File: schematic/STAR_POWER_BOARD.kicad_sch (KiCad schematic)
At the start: 62 parts, among them J1 1017491, J14 1017491, J19 6120XX21621_61200821621, J2 6120XX21621_61200621621, J21 6120XX21621_61200621621, Q1 CSD18540Q5B, Q2 CSD17577Q3A, Q3 CSD17577Q3A, Q4 CSD18540Q5B, U1 TPS566238PRQFR, U2 TPS566238PRQFR, U3 TPS40305DRCT

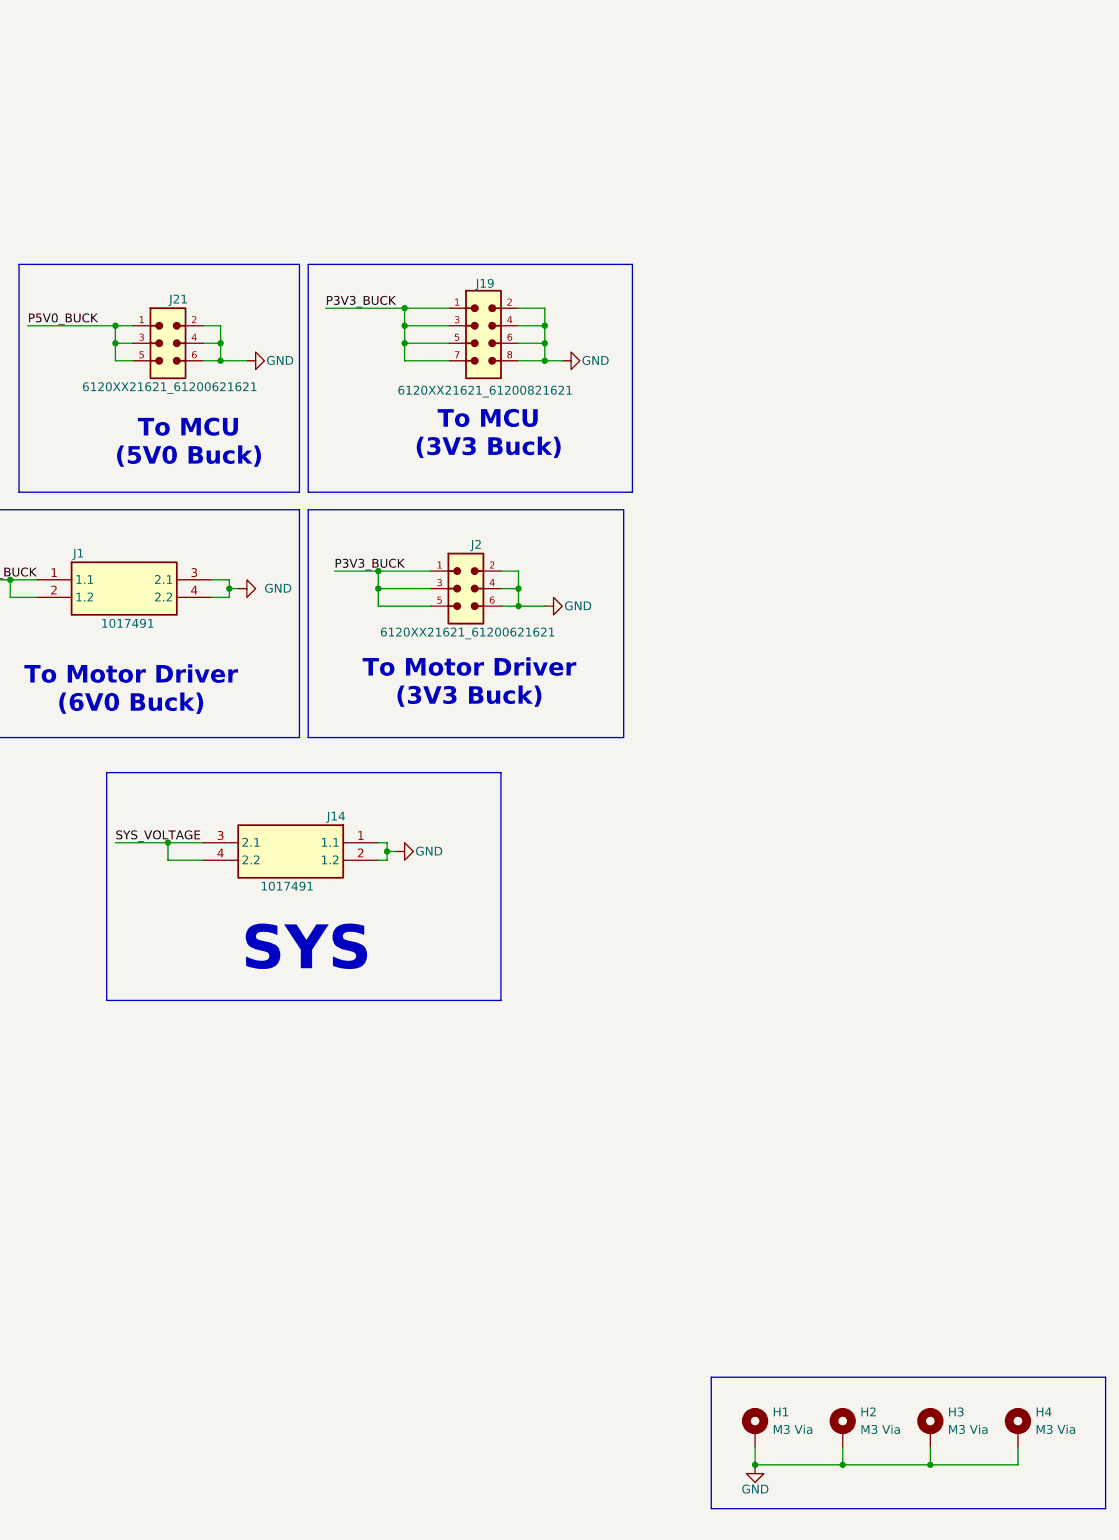
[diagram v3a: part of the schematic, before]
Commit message: Add missing footprint libraries and fix schematic references
Register three missing footprint libraries in fp-lib-table:
- DNK0008A (transistor package)
- INDPM110100X400N (inductor package)
- Q3A (transistor package)

Update STAR_POWER_BOARD schematic to use library-prefixed footprint references:
- L3: INDPM110100X400N:INDPM110100X400N
- Q1, Q4: DNK0008A:DNK0008A
- Q2, Q3: Q3A:Q3A

Fixes "footprint not found" errors during PCB update.
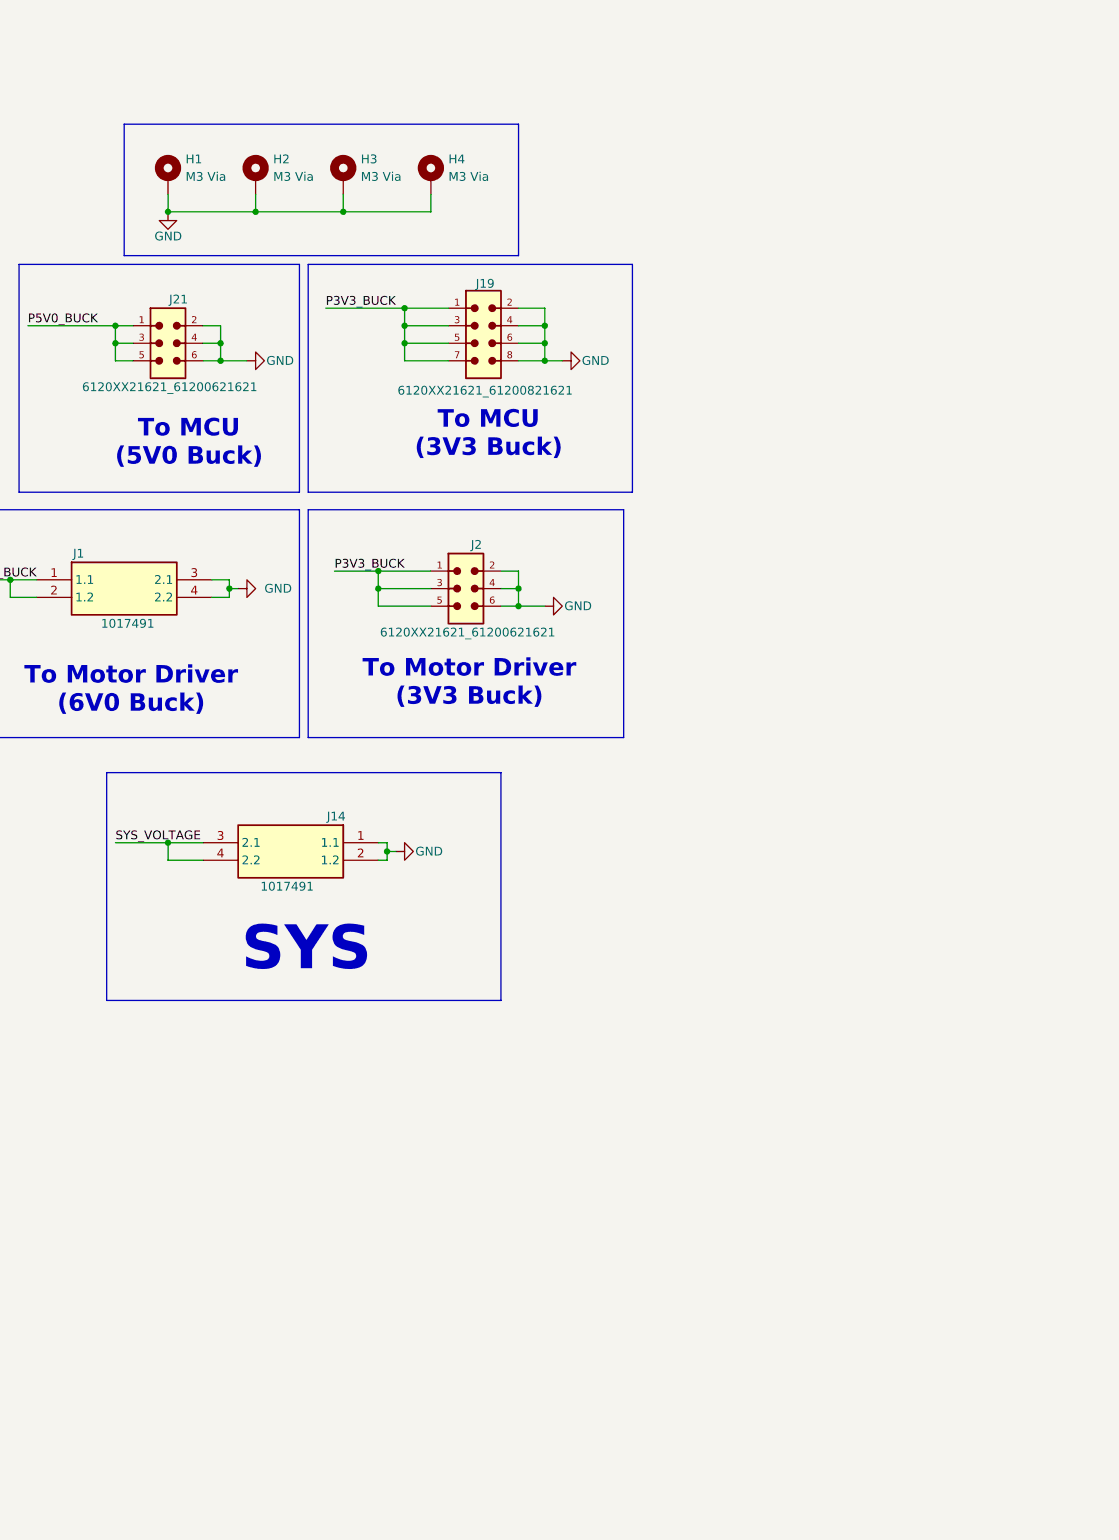
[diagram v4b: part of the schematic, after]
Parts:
- C33: footprint CAPC7866X950N:CAPC7866X950N -> CAPC7866X950N
- L3: footprint INDPM110100X400N -> INDPM110100X400N:INDPM110100X400N
- Q1, Q4: footprint DNK0008A -> DNK0008A:DNK0008A
- Q2, Q3: footprint Q3A -> Q3A:Q3A
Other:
- moved on the sheet: H1, H2, H3, H4
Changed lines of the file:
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@@
 	)
 	(rectangle
-		(start 347.98 229.87)
-		(end 405.13 248.92)
+		(start 262.89 48.26)
+		(end 320.04 67.31)
 		(stroke
 			(width 0)
@@
 	)
 	(junction
-		(at 354.33 242.57)
+		(at 269.24 60.96)
 		(diameter 0)
 		(color 0 0 0 0)
@@
 	)
 	(junction
-		(at 379.73 242.57)
+		(at 294.64 60.96)
 		(diameter 0)
 		(color 0 0 0 0)
@@
 	)
 	(junction
-		(at 367.03 242.57)
+		(at 281.94 60.96)
 		(diameter 0)
 		(color 0 0 0 0)
@@
 	(wire
 		(pts
-			(xy 392.43 240.03) (xy 392.43 242.57)
+			(xy 307.34 58.42) (xy 307.34 60.96)
 		)
 		(stroke
@@
 	(wire
 		(pts
-			(xy 354.33 240.03) (xy 354.33 242.57)
+			(xy 269.24 58.42) (xy 269.24 60.96)
 		)
 		(stroke
@@
 	(wire
 		(pts
-			(xy 367.03 242.57) (xy 354.33 242.57)
+			(xy 281.94 60.96) (xy 269.24 60.96)
 		)
 		(stroke
@@
 	(wire
 		(pts
-			(xy 392.43 242.57) (xy 379.73 242.57)
+			(xy 307.34 60.96) (xy 294.64 60.96)
 		)
 		(stroke
@@
 	(wire
 		(pts
-			(xy 367.03 242.57) (xy 379.73 242.57)
+			(xy 281.94 60.96) (xy 294.64 60.96)
 		)
 		(stroke
@@
 	(wire
 		(pts
-			(xy 379.73 240.03) (xy 379.73 242.57)
+			(xy 294.64 58.42) (xy 294.64 60.96)
 		)
 		(stroke
@@
 	(wire
 		(pts
-			(xy 367.03 240.03) (xy 367.03 242.57)
+			(xy 281.94 58.42) (xy 281.94 60.96)
 		)
 		(stroke
@@
 	(symbol
 		(lib_id "power:GND")
-		(at 354.33 242.57 0)
+		(at 269.24 60.96 0)
 		(unit 1)
 		(exclude_from_sim no)
@@
 		(dnp no)
 		(property "Reference" "#PWR01"
-			(at 354.33 248.92 0)
+			(at 269.24 67.31 0)
 			(effects
 				(font
@@
 		)
 		(property "Value" "GND"
-			(at 356.362 246.126 0)
+			(at 271.272 64.516 0)
 			(effects
 				(font
@@
 		)
 		(property "Footprint" ""
-			(at 354.33 242.57 0)
+			(at 269.24 60.96 0)
 			(effects
 				(font
@@
 		)
 		(property "Datasheet" ""
-			(at 354.33 242.57 0)
+			(at 269.24 60.96 0)
 			(effects
 				(font
@@
 		)
 		(property "Description" "Power symbol creates a global label with name \"GND\" , ground"
-			(at 354.33 242.57 0)
+			(at 269.24 60.96 0)
 			(effects
 				(font
@@
 			)
 		)
-		(property "Footprint" "Q3A"
+		(property "Footprint" "Q3A:Q3A"
 			(at 154.94 317.17 0)
 			(effects
@@
 	(symbol
 		(lib_id "Mechanical:MountingHole_Pad")
-		(at 367.03 237.49 0)
+		(at 281.94 55.88 0)
 		(unit 1)
 		(exclude_from_sim no)
@@
 		(fields_autoplaced yes)
 		(property "Reference" "H2"
-			(at 369.57 234.9499 0)
+			(at 284.48 53.3399 0)
 			(effects
 				(font
@@
 		)
 		(property "Value" "M3 Via"
-			(at 369.57 237.4899 0)
+			(at 284.48 55.8799 0)
 			(effects
 				(font
@@
 		)
 		(property "Footprint" "MountingHole:MountingHole_3.2mm_M3_Pad_Via"
-			(at 367.03 237.49 0)
+			(at 281.94 55.88 0)
 			(effects
 				(font
@@
 		)
 		(property "Datasheet" "~"
-			(at 367.03 237.49 0)
+			(at 281.94 55.88 0)
 			(effects
 				(font
@@
 		)
 		(property "Description" "Mounting Hole with connection"
-			(at 367.03 237.49 0)
+			(at 281.94 55.88 0)
 			(effects
 				(font
@@
 		)
 		(property "SNAPEDA_PN" ""
-			(at 367.03 237.49 0)
+			(at 281.94 55.88 0)
 			(effects
 				(font
@@
 		)
 		(property "Sim.Type" ""
-			(at 367.03 237.49 0)
+			(at 281.94 55.88 0)
 			(effects
 				(font
@@
 	(symbol
 		(lib_id "Mechanical:MountingHole_Pad")
-		(at 392.43 237.49 0)
+		(at 307.34 55.88 0)
 		(unit 1)
 		(exclude_from_sim no)
@@
 		(fields_autoplaced yes)
 		(property "Reference" "H4"
-			(at 394.97 234.9499 0)
+			(at 309.88 53.3399 0)
 			(effects
 				(font
@@
 		)
 		(property "Value" "M3 Via"
-			(at 394.97 237.4899 0)
+			(at 309.88 55.8799 0)
 			(effects
 				(font
@@
 		)
 		(property "Footprint" "MountingHole:MountingHole_3.2mm_M3_Pad_Via"
-			(at 392.43 237.49 0)
+			(at 307.34 55.88 0)
 			(effects
 				(font
@@
 		)
 		(property "Datasheet" "~"
-			(at 392.43 237.49 0)
+			(at 307.34 55.88 0)
 			(effects
 				(font
@@
 		)
 		(property "Description" "Mounting Hole with connection"
-			(at 392.43 237.49 0)
+			(at 307.34 55.88 0)
 			(effects
 				(font
@@
 		)
 		(property "SNAPEDA_PN" ""
-			(at 392.43 237.49 0)
+			(at 307.34 55.88 0)
 			(effects
 				(font
@@
 		)
 		(property "Sim.Type" ""
-			(at 392.43 237.49 0)
+			(at 307.34 55.88 0)
 			(effects
 				(font
@@
 	(symbol
 		(lib_id "Mechanical:MountingHole_Pad")
-		(at 379.73 237.49 0)
+		(at 294.64 55.88 0)
 		(unit 1)
 		(exclude_from_sim no)
@@
 		(fields_autoplaced yes)
 		(property "Reference" "H3"
-			(at 382.27 234.9499 0)
+			(at 297.18 53.3399 0)
 			(effects
 				(font
@@
 		)
 		(property "Value" "M3 Via"
-			(at 382.27 237.4899 0)
+			(at 297.18 55.8799 0)
 			(effects
 				(font
@@
 		)
 		(property "Footprint" "MountingHole:MountingHole_3.2mm_M3_Pad_Via"
-			(at 379.73 237.49 0)
+			(at 294.64 55.88 0)
 			(effects
 				(font
@@
 		)
 		(property "Datasheet" "~"
-			(at 379.73 237.49 0)
+			(at 294.64 55.88 0)
 			(effects
 				(font
@@
 		)
 		(property "Description" "Mounting Hole with connection"
-			(at 379.73 237.49 0)
+			(at 294.64 55.88 0)
 			(effects
 				(font
@@
 		)
 		(property "SNAPEDA_PN" ""
-			(at 379.73 237.49 0)
+			(at 294.64 55.88 0)
 			(effects
 				(font
@@
 		)
 		(property "Sim.Type" ""
-			(at 379.73 237.49 0)
+			(at 294.64 55.88 0)
 			(effects
 				(font
@@
 			)
 		)
-		(property "Footprint" "INDPM110100X400N"
+		(property "Footprint" "INDPM110100X400N:INDPM110100X400N"
 			(at 166.37 201.93 0)
 			(effects
@@
 			)
 		)
-		(property "Footprint" "CAPC7866X950N:CAPC7866X950N"
+		(property "Footprint" "CAPC7866X950N"
 			(at 199.0852 229.87 0)
 			(effects
@@
 			)
 		)
-		(property "Footprint" "DNK0008A"
+		(property "Footprint" "DNK0008A:DNK0008A"
 			(at 175.26 286.69 0)
 			(effects
@@
 			)
 		)
-		(property "Footprint" "DNK0008A"
+		(property "Footprint" "DNK0008A:DNK0008A"
 			(at 154.94 286.69 0)
 			(effects
@@
 			)
 		)
-		(property "Footprint" "Q3A"
+		(property "Footprint" "Q3A:Q3A"
 			(at 170.18 308.28 0)
 			(effects
@@
 	(symbol
 		(lib_id "Mechanical:MountingHole_Pad")
-		(at 354.33 237.49 0)
+		(at 269.24 55.88 0)
 		(unit 1)
 		(exclude_from_sim no)
@@
 		(fields_autoplaced yes)
 		(property "Reference" "H1"
-			(at 356.87 234.9499 0)
+			(at 271.78 53.3399 0)
 			(effects
 				(font
@@
 		)
 		(property "Value" "M3 Via"
-			(at 356.87 237.4899 0)
+			(at 271.78 55.8799 0)
 			(effects
 				(font
@@
 		)
 		(property "Footprint" "MountingHole:MountingHole_3.2mm_M3_Pad_Via"
-			(at 354.33 237.49 0)
+			(at 269.24 55.88 0)
 			(effects
 				(font
@@
 		)
 		(property "Datasheet" "~"
-			(at 354.33 237.49 0)
+			(at 269.24 55.88 0)
 			(effects
 				(font
@@
 		)
 		(property "Description" "Mounting Hole with connection"
-			(at 354.33 237.49 0)
+			(at 269.24 55.88 0)
 			(effects
 				(font
@@
 		)
 		(property "SNAPEDA_PN" ""
-			(at 354.33 237.49 0)
+			(at 269.24 55.88 0)
 			(effects
 				(font
@@
 		)
 		(property "Sim.Type" ""
-			(at 354.33 237.49 0)
+			(at 269.24 55.88 0)
 			(effects
 				(font

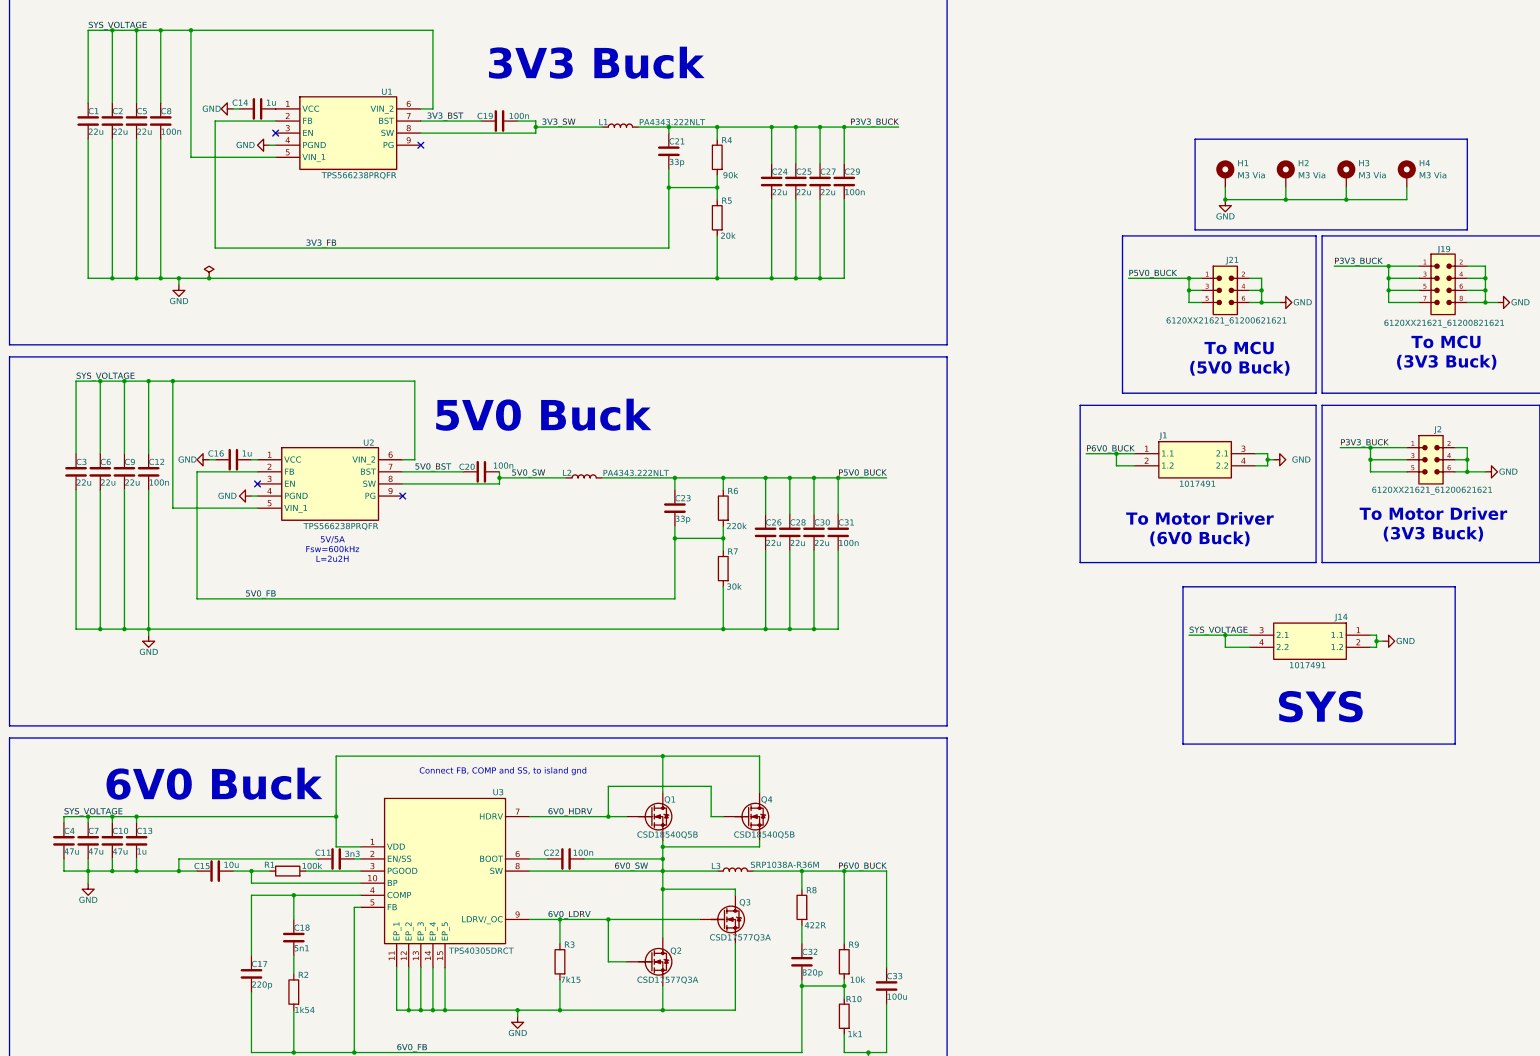
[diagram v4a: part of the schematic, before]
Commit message: fixed BMS Power Board except for 1 no connection
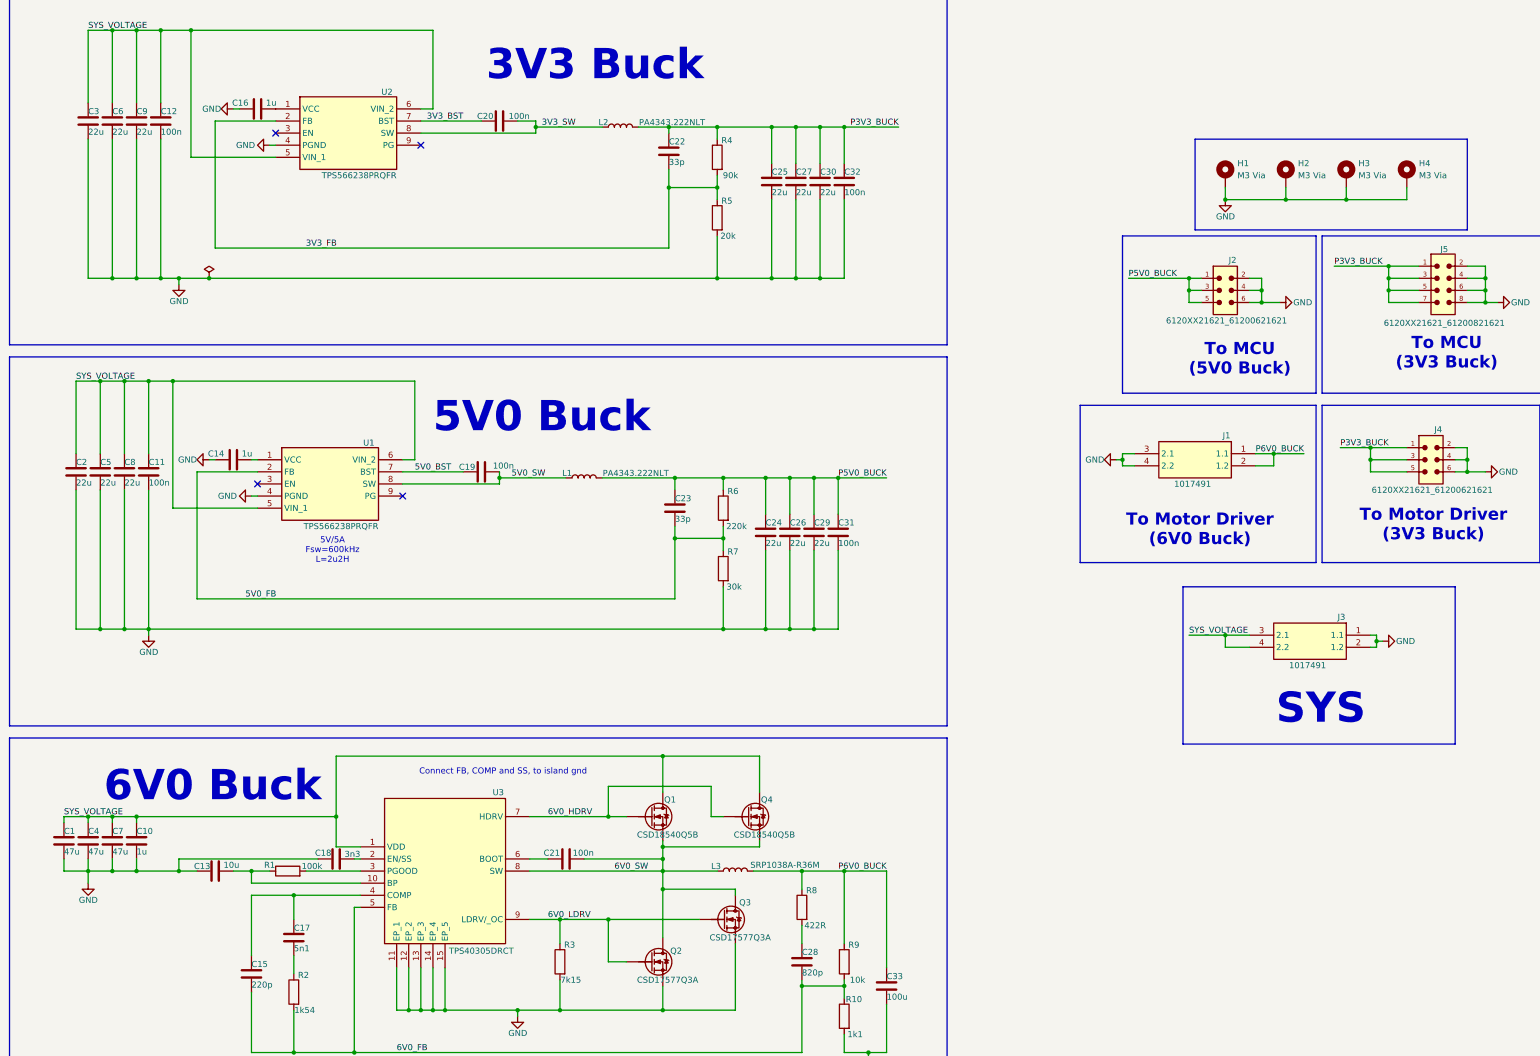
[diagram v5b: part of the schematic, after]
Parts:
- J1: DigiKey Link https://www.digikey.com/short/297znmhj -> https://www.digikey.com/short/59db1d2h; Mouser Link https://mou.sr/4pNdQFk -> https://mou.sr/4rK6010; Mouser Price per Unit 0.72 -> 0.72
- renumbered C4 to C1, C13 to C10, C12 to C11, C8 to C12, C15 to C13, C16 to C14, C17 to C15, C14 to C16, C18 to C17, C11 to C18, C20 to C19, C3 to C2, C19 to C20, C22 to C21, C21 to C22, C26 to C24, C24 to C25, C28 to C26, C25 to C27, C32 to C28, C30 to C29, C1 to C3, C27 to C30, C29 to C32, C7 to C4, C6 to C5, C2 to C6, C10 to C7, C9 to C8, C5 to C9, J21 to J2, J14 to J3, J2 to J4, J19 to J5, L2 to L1, L1 to L2, U2 to U1, U1 to U2
